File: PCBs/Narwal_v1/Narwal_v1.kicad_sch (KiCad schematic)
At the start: 67 parts, among them IC1 SWITCH-HSWA4-63DR+, IC2 SWITCH-HSWA4-63DR+, J1 SMA-LPRS-CONNECTOR, J2 Conn_01x04, J3 Conn_01x04, SW1 SW_SPST, U1 HMC452ST89ETR, U2 PGA-103+, U3 RFM96W-433S2, U4 DS3231M

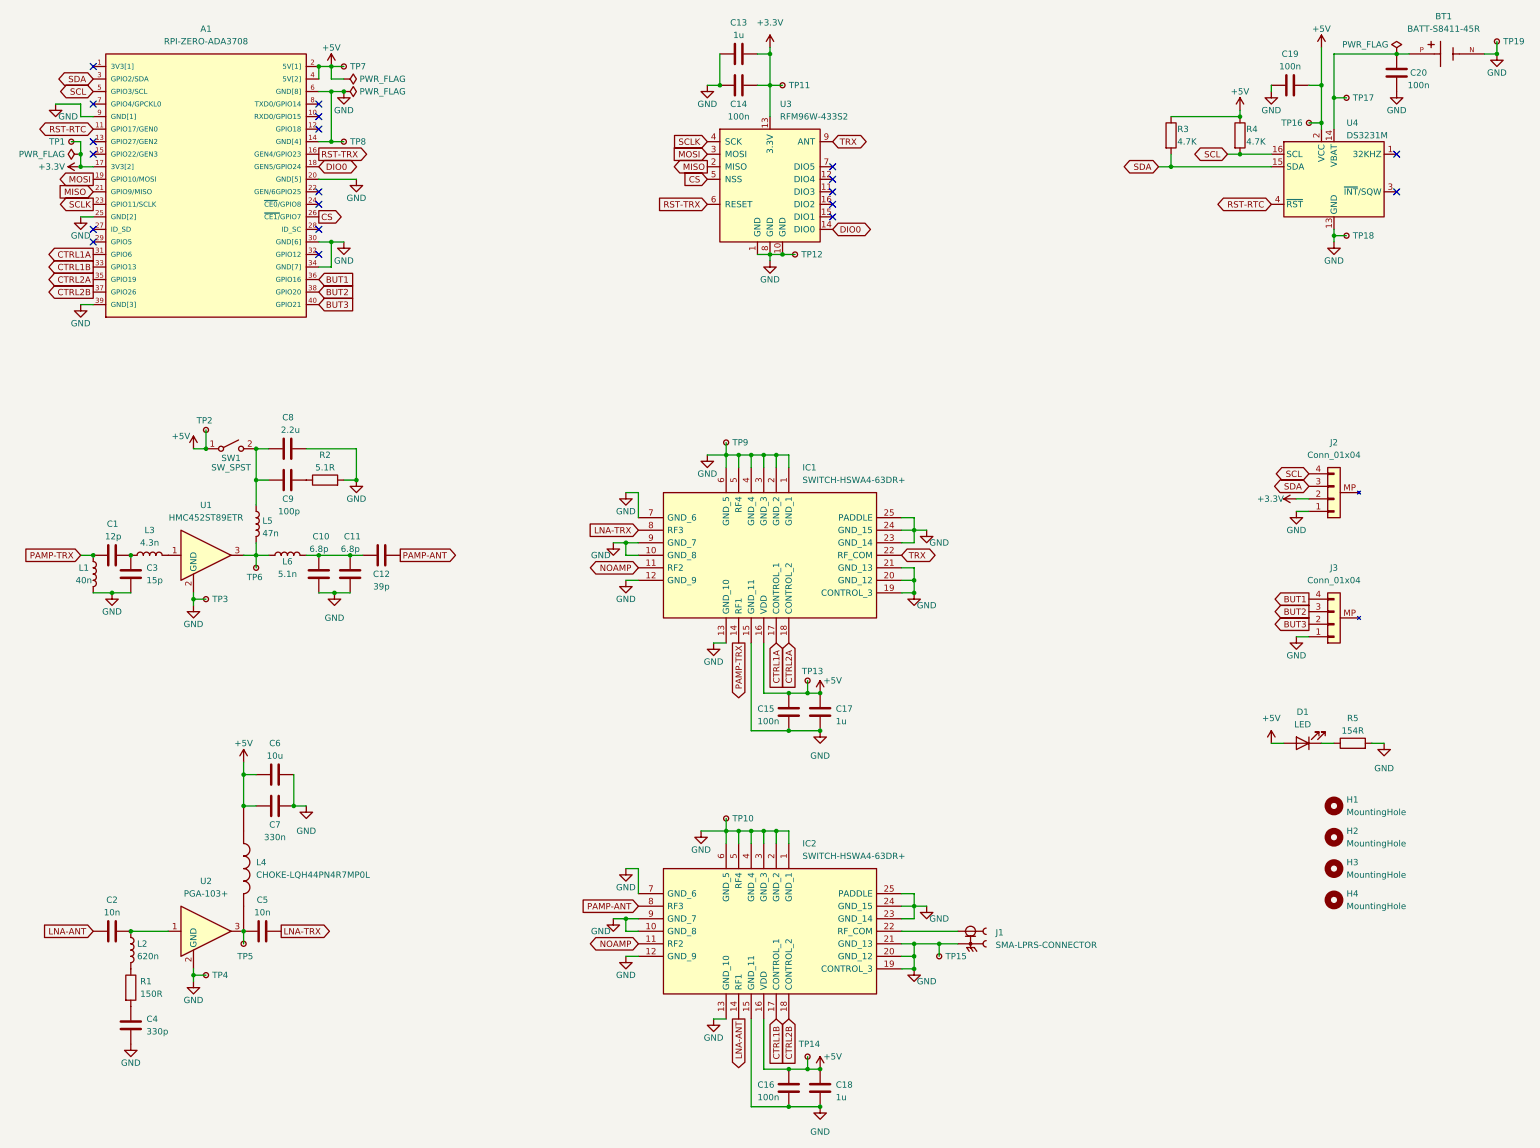
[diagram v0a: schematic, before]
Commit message: power switch fixes, JLC compatibility changes
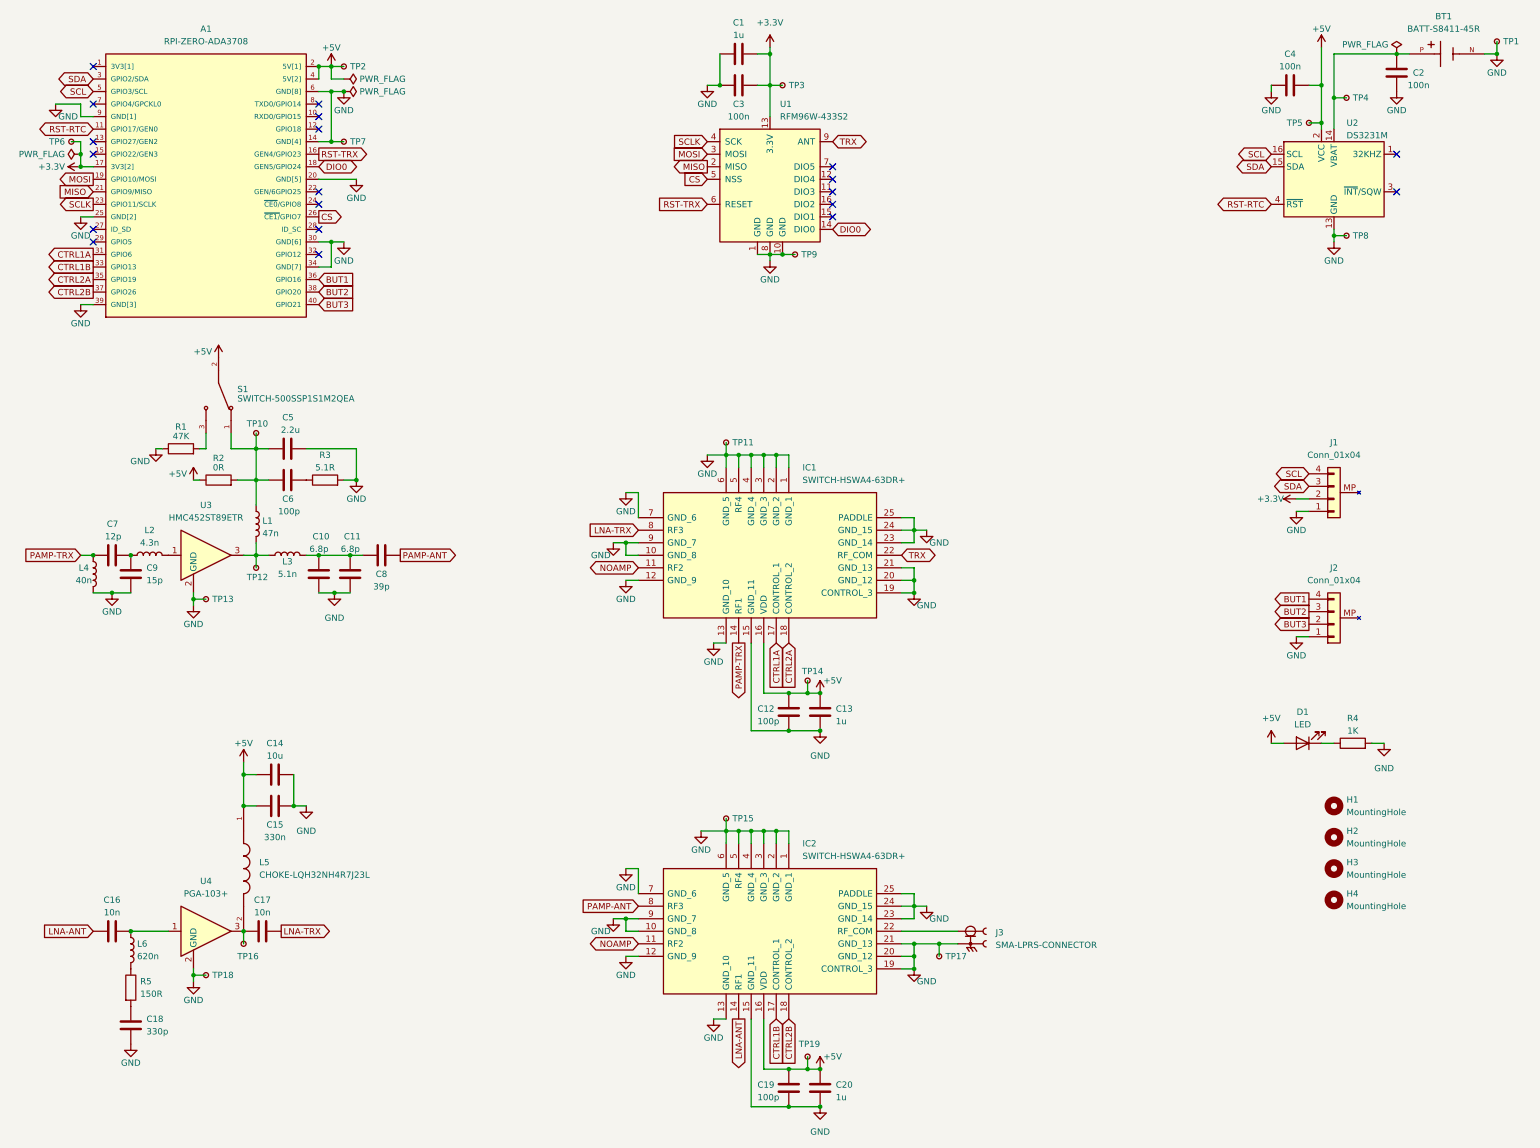
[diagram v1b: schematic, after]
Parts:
- removed L4: CHOKE-LQH44PN4R7MP0L, Eclipse_RF_Footprints:CHOKE-LQH44PN4R7MP0L, symbol Eclipse_RF_Symbols:CHOKE-LQH44PN4R7MP0L
- removed R3, R4: 4.7K, Resistor_SMD:R_1206_3216Metric, symbol Device:R
- removed SW1: SW_SPST, Button_Switch_THT:SW_Push_2P1T_Toggle_CK_PVA1xxH1xxxxxxV2, symbol Switch:SW_SPST
- added L5: CHOKE-LQH32NH4R7J23L, Eclipse_RF_Footprints:CHOKE-LQH32NH4R7J23L, symbol Eclipse_RF_Symbols:CHOKE-LQH32NH4R7J23L
- added R1: 47K, Resistor_SMD:R_1206_3216Metric, symbol Device:R
- added R2: 0R, Resistor_SMD:R_1206_3216Metric, symbol Device:R
- added S1: SWITCH-500SSP1S1M2QEA, SW_500SSP1S2M2QEA, symbol Eclipse_RF_Symbols:SWITCH-500SSP1S1M2QEA
- C12: renamed from C15; value 100n -> 100p
- C19: renamed from C16; value 100n -> 100p
- H1, H2, H3, H4: footprint MountingHole:MountingHole_2.5mm -> MountingHole:MountingHole_2.5mm_Pad
- R4: renamed from R5; value 154R -> 1K
- renumbered C13 to C1, C17 to C13, C6 to C14, C7 to C15, C2 to C16, C5 to C17, C4 to C18, C20 to C2, C18 to C20, C14 to C3, C19 to C4, C8 to C5, C9 to C6, C1 to C7, C12 to C8, C3 to C9, J2 to J1, J3 to J2, J1 to J3, L5 to L1, L3 to L2, L6 to L3, L1 to L4, L2 to L6, R2 to R3, R1 to R5, TP19 to TP1, TP2 to TP10, TP9 to TP11, TP6 to TP12, TP3 to TP13, TP13 to TP14, TP10 to TP15, TP5 to TP16, TP15 to TP17, TP4 to TP18, TP14 to TP19, TP7 to TP2, TP11 to TP3, TP17 to TP4, TP16 to TP5, TP1 to TP6, TP8 to TP7, TP18 to TP8, TP12 to TP9, U3 to U1, U4 to U2, U1 to U3, U2 to U4
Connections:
- net +5V: now also L5.1, R2.1, S1.2; no longer TP10.1
- net GND: now also R1.1
- net at C5.1, C6.1, L1.1: now also TP10.1, R2.2, S1.1
- net at C17.1, TP16.1, U4.3: now also L5.2
- new net: R1.2, S1.3
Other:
- moved on the sheet: TP10

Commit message: JLC-required silkscreen changes
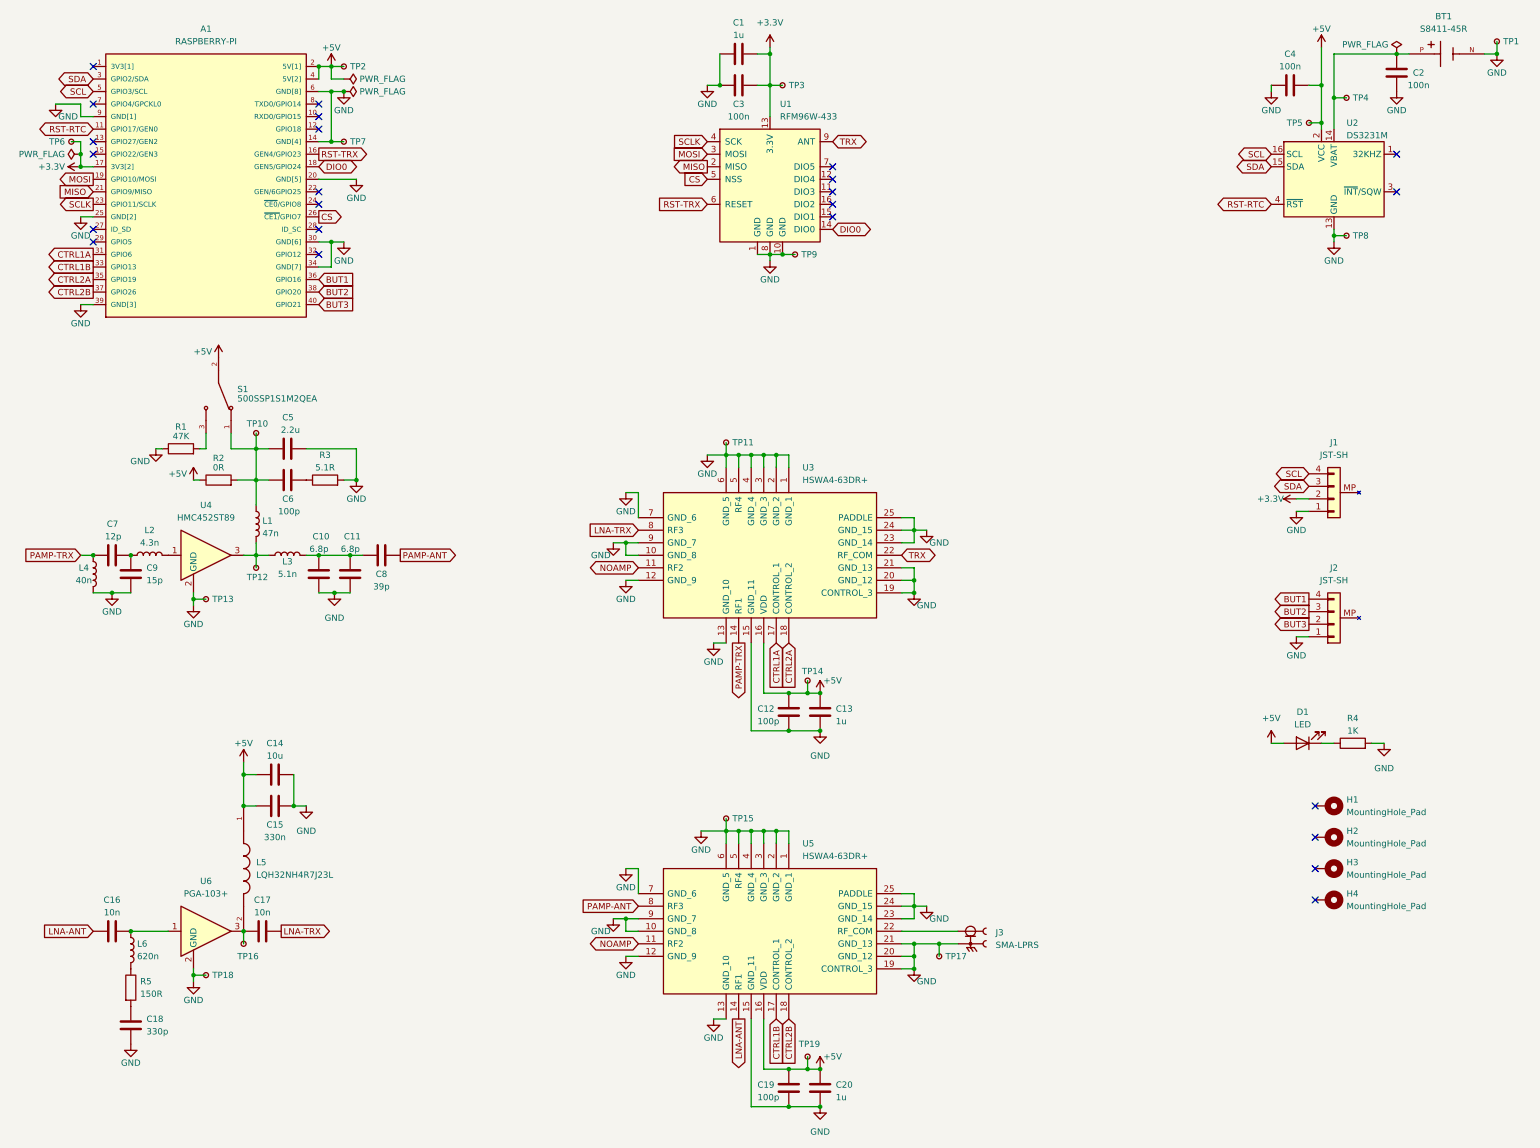
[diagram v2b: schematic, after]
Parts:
- A1: value RPI-ZERO-ADA3708 -> RASPBERRY-PI
- BT1: value BATT-S8411-45R -> S8411-45R
- H1, H2, H3, H4: value MountingHole -> MountingHole_Pad; symbol Mechanical:MountingHole -> Mechanical:MountingHole_Pad
- J1, J2: value Conn_01x04 -> JST-SH; symbol Connector_Generic:Conn_01x04 -> Eclipse_RF_Symbols:CONN-JST-SH
- J3: value SMA-LPRS-CONNECTOR -> SMA-LPRS
- L5: value CHOKE-LQH32NH4R7J23L -> LQH32NH4R7J23L
- S1: value SWITCH-500SSP1S1M2QEA -> 500SSP1S1M2QEA; footprint SW_500SSP1S2M2QEA -> Eclipse_RF_Footprints:SWITCH-500SSP1S1M2QEA
- TP10, TP11, TP12, TP13, TP14, TP15, TP16, TP17, TP18, TP19, TP2, TP3, TP4, TP5, TP6, TP7, TP8, TP9: now left out of the parts list
- U1: value RFM96W-433S2 -> RFM96W-433
- U3: renamed from IC1; value SWITCH-HSWA4-63DR+ -> HSWA4-63DR+
- U4: renamed from U3; value HMC452ST89ETR -> HMC452ST89
- U5: renamed from IC2; value SWITCH-HSWA4-63DR+ -> HSWA4-63DR+
- renumbered U4 to U6
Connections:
- no-connect marks 20 -> 24

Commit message: final changes and fabrication
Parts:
- removed R1: 47K, Resistor_SMD:R_1206_3216Metric, symbol Device:R
- D1: value LED -> PWR; footprint LED_THT:LED_D3.0mm -> LED_THT:LED_D5.0mm
- L2, L3: footprint Inductor_SMD:L_1210_3225Metric -> Inductor_SMD:L_0603_1608Metric_Pad1.05x0.95mm_HandSolder
- renumbered R2 to R1, R3 to R2, R4 to R3, R5 to R4
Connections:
- no-connect marks 24 -> 25
